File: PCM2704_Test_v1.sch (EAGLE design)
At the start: 50 parts, among them IC1 REG1117, IC2 REG1117, X1 USB-MB-S

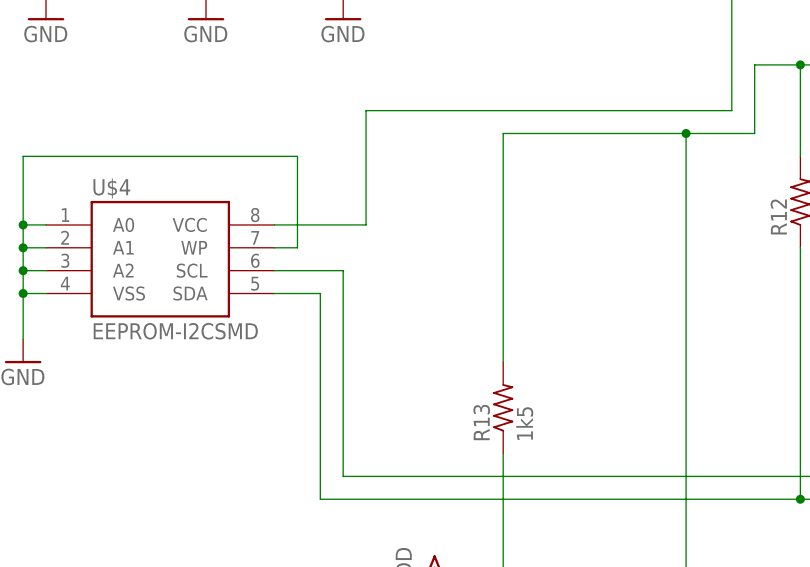
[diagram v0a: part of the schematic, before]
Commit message: Small changes made
Wired up the SDA and SCL for the EEPROM. Also added a bypass cap to the
EEPROM.
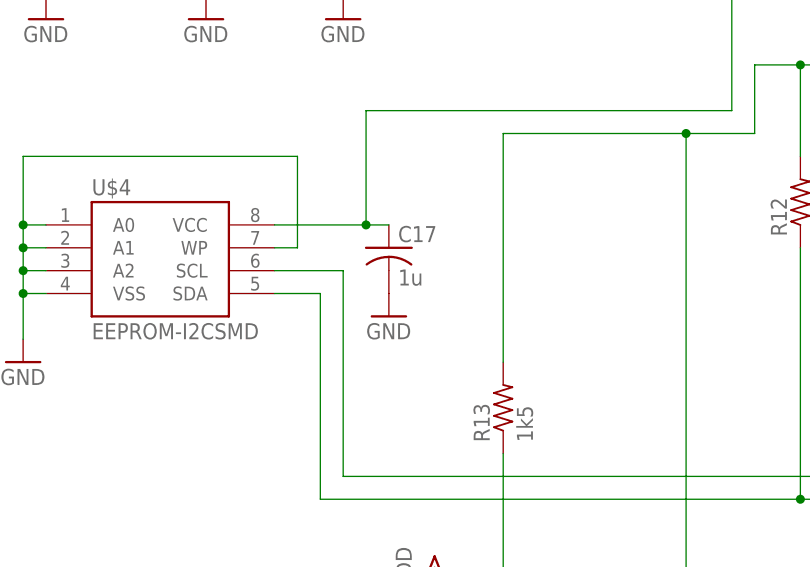
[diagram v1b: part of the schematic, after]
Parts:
- added C17: 1u, rcl:C-USC0402
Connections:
- net GND: now also C17.2
- net VDD: now also C17.1
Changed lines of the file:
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@@
 <part name="GND25" library="SparkFun" deviceset="GND" device=""/>
 <part name="R12" library="rcl" deviceset="R-US_" device="R0603" value="1k5"/>
+<part name="C17" library="rcl" deviceset="C-US" device="C0402" value="1u"/>
+<part name="GND17" library="SparkFun" deviceset="GND" device=""/>
 </parts>
 <sheets>
@@
 <instance part="GND25" gate="1" x="-60.96" y="76.2"/>
 <instance part="R12" gate="G$1" x="25.4" y="93.98" rot="R90"/>
+<instance part="C17" gate="G$1" x="-20.32" y="88.9"/>
+<instance part="GND17" gate="1" x="-20.32" y="81.28"/>
 </instances>
 <busses>
@@
 <junction x="-60.96" y="91.44"/>
 <pinref part="GND25" gate="1" pin="GND"/>
+</segment>
+<segment>
+<pinref part="C17" gate="G$1" pin="2"/>
+<pinref part="GND17" gate="1" pin="GND"/>
 </segment>
 </net>
@@
 <wire x1="-22.86" y1="91.44" x2="-33.02" y2="91.44" width="0.1524" layer="91"/>
 <wire x1="2.54" y1="119.38" x2="17.78" y2="119.38" width="0.1524" layer="91"/>
-</segment>
-<segment>
+<pinref part="C17" gate="G$1" pin="1"/>
+<wire x1="-20.32" y1="91.44" x2="-22.86" y2="91.44" width="0.1524" layer="91"/>
+<junction x="-22.86" y="91.44"/>
+</segment>
+<segment>
